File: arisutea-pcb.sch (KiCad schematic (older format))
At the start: 54 parts, among them J12 VCC, J13 D+, J14 D-, J15 GND, J16 RGB, J17 RGB_IN, J18 RGB_OUT, J2 MISO, J3 +5V, J4 SCK, J5 MOSI, J6 ~RES~, J7 GND, U1 USBLC6-2SC6, U2 ATmega32U4-AU, Y1 Crystal_GND24

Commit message: v0.6.3
- Updated mounting holes for new case design.
- Removed matte case as the regular file can be used for either.
- Library update.
- Gerbies regenerated for version bump.
- iBOM added.
- README for most pages edited.
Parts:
- H1, H2, H3, H4, H5, H6, H7, H8: footprint arisutea:Plated_Through_Hole_M2 -> arisutea:Generic-Mounthole
- LOGO1, LOGO2: symbol arisutea-pcb-r1:arisutea_logo -> arisutea-pcb-r1:LOGO
- LOGO3, LOGO4: value arisutea_logo -> QMK Logo; footprint Symbol:OSHW-Logo_5.7x6mm_SilkScreen -> arisutea:OSHW-Logo_11.4x12mm_SilkScreen; symbol arisutea-pcb-r1:arisutea_logo -> arisutea-pcb-r1:LOGO
- LOGO5, LOGO6: footprint 3x6_graphics:QMK_Logo_Light -> arisutea:QMK_Logo_Light; symbol arisutea-pcb-r1:arisutea_logo -> arisutea-pcb-r1:LOGO
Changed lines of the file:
@@
 Sheet 1 2
 Title "Arisutea Keyboard"
-Date "2021-03-27"
-Rev "0.6"
+Date "2021-05-04"
+Rev "0.6.2"
 Comp "3x6 Design"
 Comment1 ""
@@
 F 0 "H1" H 9900 2946 50  0000 L CNN
 F 1 "ThroughHole" H 9900 2855 50  0000 L CNN
-F 2 "arisutea:Plated_Through_Hole_M2" H 9800 2900 50  0001 C CNN
+F 2 "arisutea:Generic-Mounthole" H 9800 2900 50  0001 C CNN
 F 3 "~" H 9800 2900 50  0001 C CNN
 	1    9800 2900
@@
 F 0 "H2" H 9900 3146 50  0000 L CNN
 F 1 "ThroughHole" H 9900 3055 50  0000 L CNN
-F 2 "arisutea:Plated_Through_Hole_M2" H 9800 3100 50  0001 C CNN
+F 2 "arisutea:Generic-Mounthole" H 9800 3100 50  0001 C CNN
 F 3 "~" H 9800 3100 50  0001 C CNN
 	1    9800 3100
@@
 F 0 "H3" H 9900 3346 50  0000 L CNN
 F 1 "ThroughHole" H 9900 3255 50  0000 L CNN
-F 2 "arisutea:Plated_Through_Hole_M2" H 9800 3300 50  0001 C CNN
+F 2 "arisutea:Generic-Mounthole" H 9800 3300 50  0001 C CNN
 F 3 "~" H 9800 3300 50  0001 C CNN
 	1    9800 3300
@@
 F 0 "H4" H 9900 3546 50  0000 L CNN
 F 1 "ThroughHole" H 9900 3455 50  0000 L CNN
-F 2 "arisutea:Plated_Through_Hole_M2" H 9800 3500 50  0001 C CNN
+F 2 "arisutea:Generic-Mounthole" H 9800 3500 50  0001 C CNN
 F 3 "~" H 9800 3500 50  0001 C CNN
 	1    9800 3500
@@
 F 0 "H5" H 9900 3746 50  0000 L CNN
 F 1 "ThroughHole" H 9900 3655 50  0000 L CNN
-F 2 "arisutea:Plated_Through_Hole_M2" H 9800 3700 50  0001 C CNN
+F 2 "arisutea:Generic-Mounthole" H 9800 3700 50  0001 C CNN
 F 3 "~" H 9800 3700 50  0001 C CNN
 	1    9800 3700
@@
 F 0 "H6" H 9900 3946 50  0000 L CNN
 F 1 "ThroughHole" H 9900 3855 50  0000 L CNN
-F 2 "arisutea:Plated_Through_Hole_M2" H 9800 3900 50  0001 C CNN
+F 2 "arisutea:Generic-Mounthole" H 9800 3900 50  0001 C CNN
 F 3 "~" H 9800 3900 50  0001 C CNN
 	1    9800 3900
@@
 F 0 "H7" H 9900 4146 50  0000 L CNN
 F 1 "ThroughHole" H 9900 4055 50  0000 L CNN
-F 2 "arisutea:Plated_Through_Hole_M2" H 9800 4100 50  0001 C CNN
+F 2 "arisutea:Generic-Mounthole" H 9800 4100 50  0001 C CNN
 F 3 "~" H 9800 4100 50  0001 C CNN
 	1    9800 4100
@@
 F 0 "H8" H 9900 4346 50  0000 L CNN
 F 1 "ThroughHole" H 9900 4255 50  0000 L CNN
-F 2 "arisutea:Plated_Through_Hole_M2" H 9800 4300 50  0001 C CNN
+F 2 "arisutea:Generic-Mounthole" H 9800 4300 50  0001 C CNN
 F 3 "~" H 9800 4300 50  0001 C CNN
 	1    9800 4300
@@
 	1750 5250 1750 6600
 $Comp
-L arisutea-pcb-r1:arisutea_logo LOGO1
+L arisutea-pcb-r1:LOGO LOGO1
 U 1 1 6042E29E
 P 8700 6100
@@
 $EndComp
 $Comp
-L arisutea-pcb-r1:arisutea_logo LOGO2
+L arisutea-pcb-r1:LOGO LOGO2
 U 1 1 605B7585
 P 9050 6100
@@
 FN_L
 $Comp
-L arisutea-pcb-r1:arisutea_logo LOGO3
+L arisutea-pcb-r1:LOGO LOGO3
 U 1 1 6062F214
 P 9400 6100
 F 0 "LOGO3" H 9400 6300 50  0000 C CNN
-F 1 "arisutea_logo" H 9475 6474 50  0001 C CNN
-F 2 "Symbol:OSHW-Logo_5.7x6mm_SilkScreen" H 9400 6450 50  0001 C CNN
+F 1 "QMK Logo" H 9475 6474 50  0001 C CNN
+F 2 "arisutea:OSHW-Logo_11.4x12mm_SilkScreen" H 9400 6450 50  0001 C CNN
 F 3 "" H 9400 6450 50  0001 C CNN
 	1    9400 6100
@@
 $EndComp
 $Comp
-L arisutea-pcb-r1:arisutea_logo LOGO4
+L arisutea-pcb-r1:LOGO LOGO4
 U 1 1 6062F624
 P 9750 6100
 F 0 "LOGO4" H 9750 6300 50  0000 C CNN
-F 1 "arisutea_logo" H 9825 6474 50  0001 C CNN
-F 2 "Symbol:OSHW-Logo_5.7x6mm_SilkScreen" H 9750 6450 50  0001 C CNN
+F 1 "QMK Logo" H 9825 6474 50  0001 C CNN
+F 2 "arisutea:OSHW-Logo_11.4x12mm_SilkScreen" H 9750 6450 50  0001 C CNN
 F 3 "" H 9750 6450 50  0001 C CNN
 	1    9750 6100
@@
 $EndComp
 $Comp
-L arisutea-pcb-r1:arisutea_logo LOGO5
+L arisutea-pcb-r1:LOGO LOGO5
 U 1 1 6063AB78
 P 10100 6100
 F 0 "LOGO5" H 10100 6300 50  0000 C CNN
 F 1 "QMK_Logo_Light" H 10175 6474 50  0001 C CNN
-F 2 "3x6_graphics:QMK_Logo_Light" H 10100 6450 50  0001 C CNN
+F 2 "arisutea:QMK_Logo_Light" H 10100 6450 50  0001 C CNN
 F 3 "" H 10100 6450 50  0001 C CNN
 	1    10100 6100
@@
 $EndComp
 $Comp
-L arisutea-pcb-r1:arisutea_logo LOGO6
+L arisutea-pcb-r1:LOGO LOGO6
 U 1 1 6063AEC9
 P 10450 6100
 F 0 "LOGO6" H 10450 6300 50  0000 C CNN
 F 1 "QMK_Logo_Light" H 10525 6474 50  0001 C CNN
-F 2 "3x6_graphics:QMK_Logo_Light" H 10450 6450 50  0001 C CNN
+F 2 "arisutea:QMK_Logo_Light" H 10450 6450 50  0001 C CNN
 F 3 "" H 10450 6450 50  0001 C CNN
 	1    10450 6100

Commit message: Version 1.0 Release
Release of version 1.

- Libraries have been merged for easier access.
- Moved one cap a little closer to the MCU.
- Regenerated gerbies, BOM and POS files.
- New iBOM.
- Bumped version number.
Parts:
- removed R1, R2: 22, arisutea:R_0805_2012Metric_Pad1.20x1.40mm_HandSolder, symbol Device:R
- removed R5, R6: 5k1, arisutea:R_0805_2012Metric_Pad1.20x1.40mm_HandSolder, symbol Device:R
- removed U1: USBLC6-2SC6, arisutea:SOT-23-6_Handsoldering, symbol arisutea-pcb-r1:USBLC6-2SC6-Power_Protection
- removed U2: ATmega32U4-AU, arisutea:TQFP-44_10x10mm_P0.8mm, symbol arisutea-pcb-r1:ATmega32U4-AU-MCU_Microchip_ATmega
- removed USB1: USB_C_HRO_TYPE-C-31-M-12-USB_Type-C, arisutea:USB_C_Receptacle_HRO_TYPE-C-31-M-12-HandSoldering, symbol arisutea-pcb-r1:USB_C_Receptacle_HRO_TYPE-C-31-M-12
- added R1, R2: 22, arisutea:R_0805_2012Metric_Pad1.20x1.40mm_HandSolder, symbol arisutea-pcb:Device_R
- added R5, R6: 5k1, arisutea:R_0805_2012Metric_Pad1.20x1.40mm_HandSolder, symbol arisutea-pcb:Device_R
- added U1: USBLC6-2SC6, arisutea:SOT-23-6_Handsoldering, symbol arisutea-pcb:USBLC6-2SC6-Power_Protection
- added U2: ATMEGA32U4_QFN44, arisutea:TQFP-44_10x10mm_P0.8mm, symbol arisutea-pcb:ATmega32U4-AU-MCU_Microchip_ATmega
- added USB1: USB_C_HRO-TYPE-C-31-M-12, arisutea:USB_C_Receptacle_HRO_TYPE-C-31-M-12-HandSoldering, symbol arisutea-pcb:USB_HRO-TYPE-C-31-M-12
- C1, C2, C3, C4, C5, C6, C7, C8, C9: symbol Device:C -> arisutea-pcb:Device_C_Small
- F1: symbol Device:Polyfuse_Small -> arisutea-pcb:Device_Polyfuse_Small; LCSC (none) -> C70068
- H1, H2, H3, H4, H5, H6, H7, H8: symbol Mechanical:MountingHole -> arisutea-pcb:Mechanical_MountingHole
- J4: value SCK -> SCLK
- LED1, LED2, LED3: symbol arisutea-pcb-r1:LED -> arisutea-pcb:LED; LCSC (none) -> C401114
- LOGO1, LOGO2, LOGO3, LOGO4, LOGO5, LOGO6: symbol arisutea-pcb-r1:LOGO -> arisutea-pcb:LOGO
- R3, R4: symbol Device:R -> arisutea-pcb:Device_R
- R7, R8, R9: LCSC (none) -> C27834
- SWR1: symbol Switch:SW_Push -> arisutea-pcb:Switch_SW_Push
- Y1: symbol Device:Crystal_GND24 -> arisutea-pcb:Device_Crystal_GND24
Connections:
- net +5V: now also C3.2, C5.2, U2.14 (VCC), U2.2 (UVCC), U2.24 (AVCC), U2.34 (VCC), U2.44 (AVCC), U2.7 (VBUS); no longer C3.1, C5.1
- net CAPS_L: now also U2.38 (ADC5/PF5)
- net D+: now also R1.1, U2.4 (D+)
- net D-: now also R2.1, U2.3 (D-)
- net FN_L: now also U2.39 (ADC4/PF4)
- net GND: now also C3.1, C4.1, C5.1, R5.1, R6.1, U1.2 (GND), U2.15 (GND), U2.23 (GND), U2.35 (GND), U2.43 (GND), U2.5 (UGND), USB1.A1 (GND), USB1.A12 (GND), USB1.S1 (SHIELD); no longer C3.2, C4.2, C5.2
- net MISO: now also U2.11 (PB3/PDO/PCINT3/MISO)
- net MOSI: now also U2.10 (PB2/PDI/PCINT2/MOSI)
- net NUM_L: now also U2.37 (ADC6/PF6)
- net RGB: now also U2.36 (ADC7/PF7)
- net VCC: now also U1.5 (VBUS), USB1.A4 (VBUS), USB1.A9 (VBUS)
- net XTAL1: now also U2.17 (XTAL1)
- net XTAL2: now also U2.16 (XTAL2)
- net col0: now also U2.41 (ADC0/PF0)
- net col1: now also U2.40 (ADC1/PF1)
- net col10: now also U2.29 (PCINT4/ADC12/PB5)
- net col11: now also U2.28 (ADC11/PCINT4/PB4)
- net col12: now also U2.27 (ADC10/T0/PD7)
- net col13: now also U2.26 (ADC9/T1/PD6)
- net col2: now also U2.1 (PE6/INT6/AIN0)
- net col3: now also U2.32 (CLK/PC7)
- net col4: now also U2.31 (PC6)
- net col5: now also U2.30 (PCINT6/ADC13/PB6)
- net col6: now also U2.25 (ADC8/PD4)
- net col8: now also U2.8 (PB0/SS/PCINT0)
- net col9: now also U2.12 (PB7/RTS)
- net row0: now also U2.18 (PD0/SCL/~INT0~)
- net row1: now also U2.19 (PD1/SDA/~INT1~)
- net row2: now also U2.20 (PD2/RDX1/~INT2~)
- net row3: now also U2.21 (PD3/TXD1/~INT3~)
- net row4: now also U2.22 (PD5/~CTS~/XCK1)
- net at R4.1: now also U2.33 (~HWB~/PE2)
- net USB+: now reaches J13.1 (Pin_1)
- net USB+: now also R2.2, U1.6 (IO1)
- net USB-: now reaches J14.1 (Pin_1)
- net USB-: now also R1.2, U1.4 (IO2)
- net SCK renamed SCLK
- net SCLK: now also U2.9 (PBI/PCINT1/SCLK)
- net ~RES~ renamed RESET
- net RESET: now also U2.13 (~RESET~)
- new net: C4.2, U2.6 (UCAP)
- new net: R5.2, USB1.A5 (CC1)
- new net: R6.2, USB1.B5 (CC2)
- new net: U1.3 (IO2), USB1.A6 (DP1), USB1.B6 (DP2)
- new net: U1.1 (IO1), USB1.A7 (DN1), USB1.B7 (DN2)
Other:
- note added: "ATMEGA32U4 MCU"
- note added: "Crystal Oscillator"
- note added: "LEDs"
- note added: "Logos"
- note added: "Mounting\nHoles"
- note added: "Reset Switch & Fuse"
- note added: "Switch Matrix"
- note added: "USB & Programming Headers"
- note added: "USB-C Connection & ESD Protection"
- moved on the sheet: C1, C2, C3, C4, C5, C6, C7, C8, C9, F1, H1, H2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

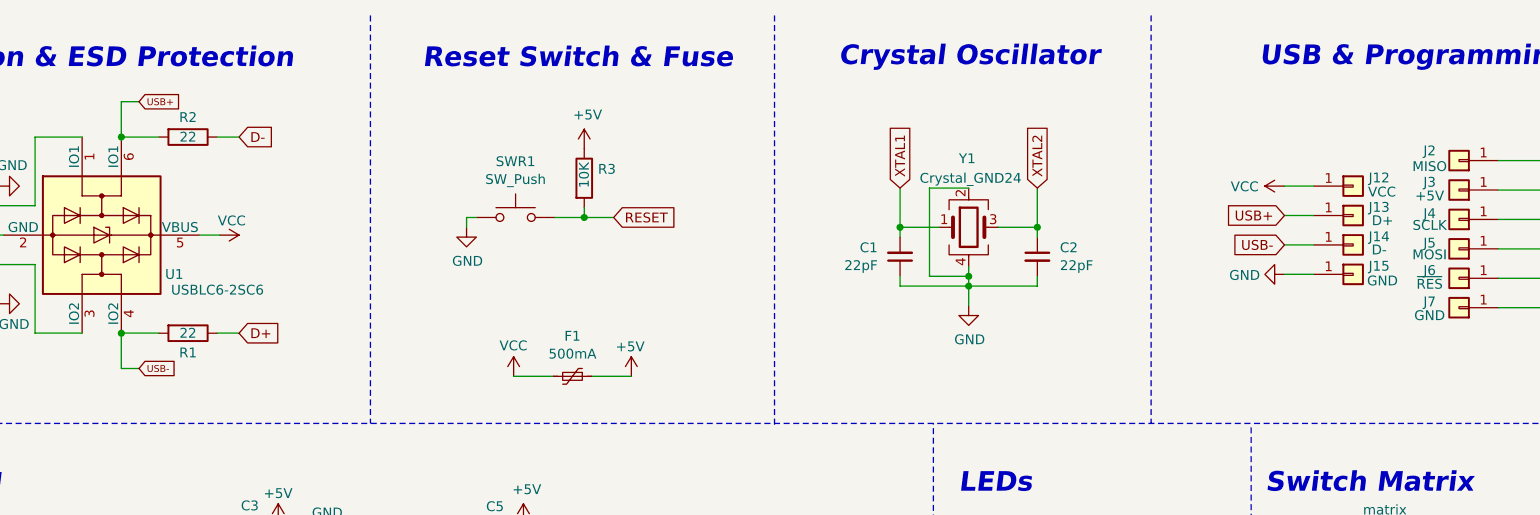
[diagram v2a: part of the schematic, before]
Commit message: fixed USB net names
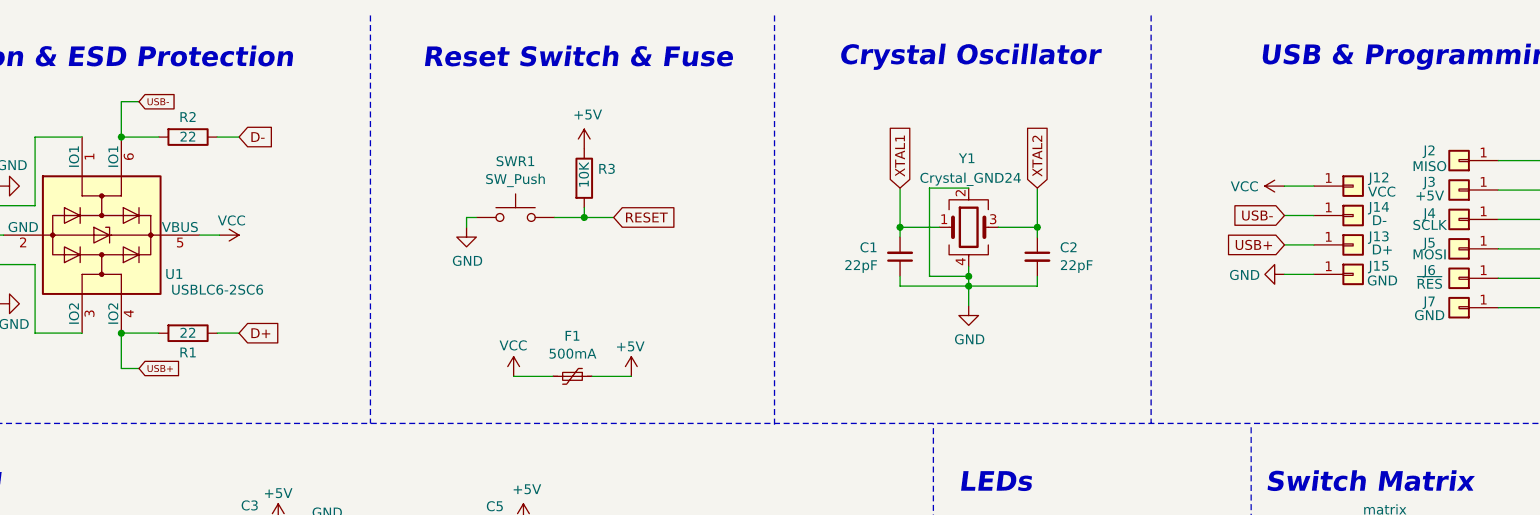
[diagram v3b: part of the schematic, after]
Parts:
- J13: renamed from J14; value D- -> D+
- J14: renamed from J13; value D+ -> D-
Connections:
- net USB+: now also J13.1 (Pin_1), R1.2, U1.4 (IO2); no longer J14.1 (Pin_1), R2.2, U1.6 (IO1)
- net USB-: now also J14.1 (Pin_1), R2.2, U1.6 (IO1); no longer J13.1 (Pin_1), R1.2, U1.4 (IO2)
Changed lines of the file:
@@
 EESchema Schematic File Version 4
+LIBS:arisutea-pcb-cache
 EELAYER 30 0
 EELAYER END
@@
 Text GLabel 2880 3570 1    50   Input ~ 0
 MOSI
+Text GLabel 2920 2280 2    35   Input ~ 0
+USB+
 Text GLabel 2920 920  2    35   Input ~ 0
-USB+
-Text GLabel 2920 2280 2    35   Input ~ 0
 USB-
 Text GLabel 3030 3570 1    50   Input ~ 0
@@
 Text GLabel 3380 6920 3    50   Input ~ 0
 col13
-Text GLabel 3430 1100 2    50   Input ~ 0
-D-
-Text GLabel 3430 2100 2    50   Input ~ 0
-D+
 Text GLabel 3630 6920 3    50   Input ~ 0
 col12
@@
 Text GLabel 7565 4475 0    50   Input ~ 0
 RGB_A
+Text GLabel 8760 1650 0    50   Input ~ 0
+USB+
 Text GLabel 8760 1500 0    50   Input ~ 0
-USB+
-Text GLabel 8760 1650 0    50   Input ~ 0
 USB-
 Text GLabel 9110 3200 0    50   Input ~ 0
@@
 $EndComp
 $Comp
-L Connector_Generic:Conn_01x01 J13
+L Connector_Generic:Conn_01x01 J14
 U 1 1 5C4E1CA1
 P 9110 1500
-F 0 "J13" H 9189 1542 50  0000 L CNN
-F 1 "D+" H 9205 1474 50  0000 L CNN
+F 0 "J14" H 9189 1542 50  0000 L CNN
+F 1 "D-" H 9205 1474 50  0000 L CNN
 F 2 "arisutea:PinHeader_1x01_P2.54mm_Vertical" H 9110 1500 50  0001 C CNN
 F 3 "~" H 9110 1500 50  0001 C CNN
@@
 $EndComp
 $Comp
-L Connector_Generic:Conn_01x01 J14
+L Connector_Generic:Conn_01x01 J13
 U 1 1 5C4F0ABE
 P 9110 1650
-F 0 "J14" H 9189 1692 50  0000 L CNN
-F 1 "D-" H 9204 1625 50  0000 L CNN
+F 0 "J13" H 9189 1692 50  0000 L CNN
+F 1 "D+" H 9204 1625 50  0000 L CNN
 F 2 "arisutea:PinHeader_1x01_P2.54mm_Vertical" H 9110 1650 50  0001 C CNN
 F 3 "~" H 9110 1650 50  0001 C CNN
@@
 Text Notes 10325 3075 0    100  Italic 20
 Mounting\nHoles
+Text GLabel 3430 2100 2    50   Input ~ 0
+D+
+Text GLabel 3430 1100 2    50   Input ~ 0
+D-
 $EndSCHEMATC
